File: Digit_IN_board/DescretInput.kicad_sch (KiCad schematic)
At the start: 55 parts, among them J11 DS1013-01-10RSiB-B (1), J12 DS0, J13 DS0

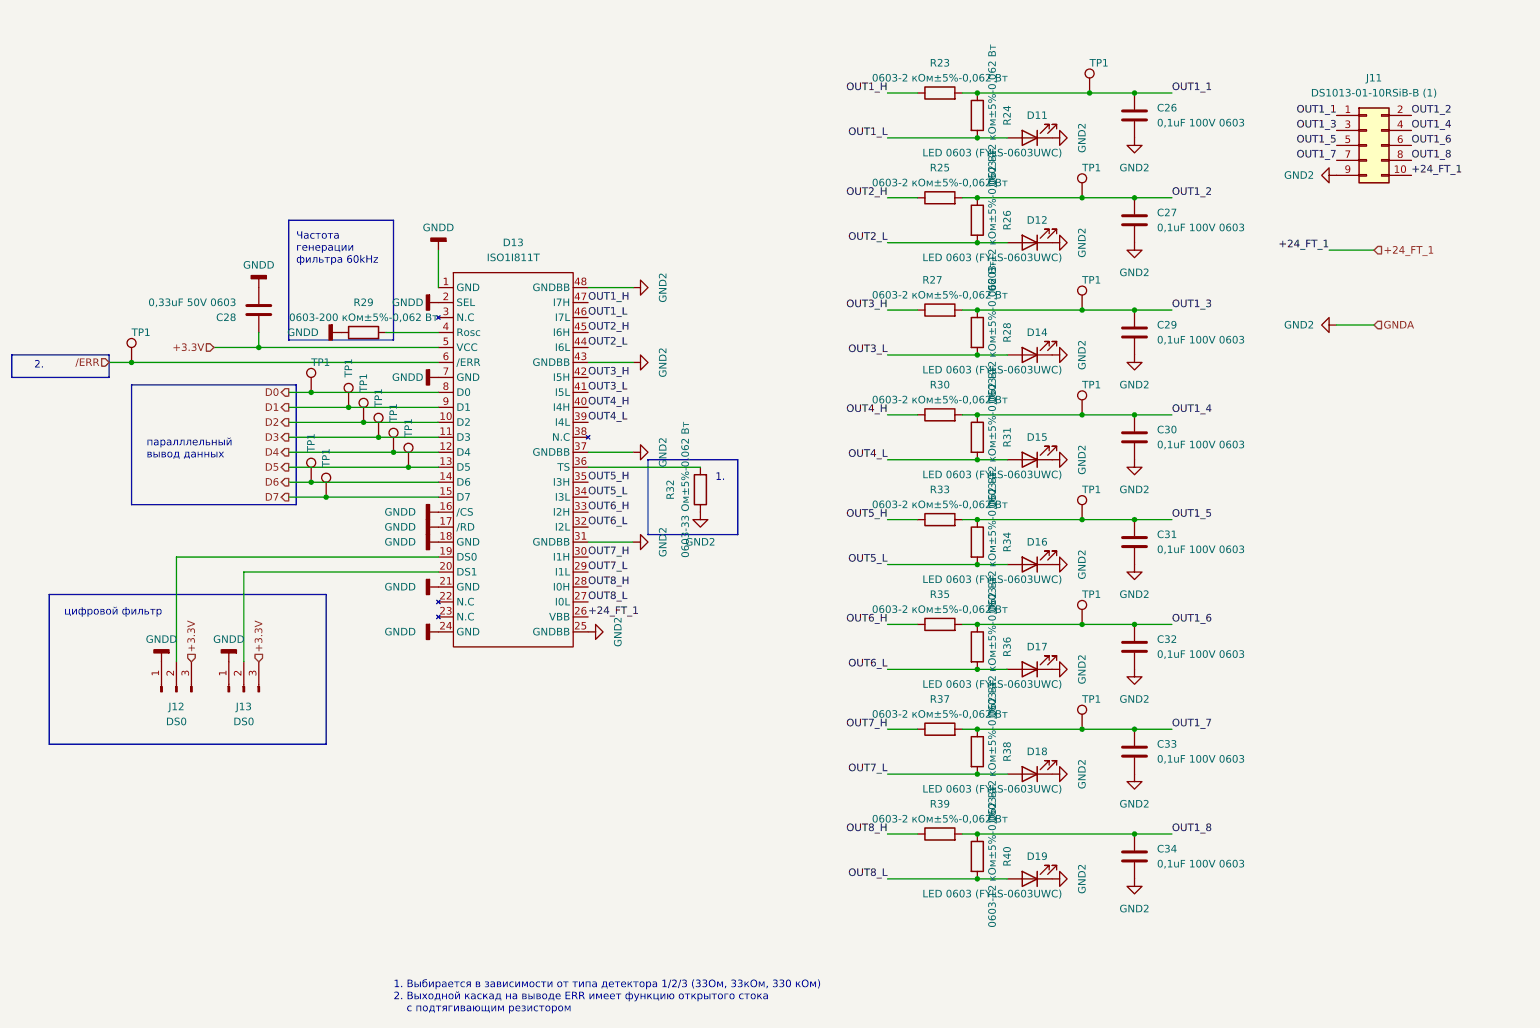
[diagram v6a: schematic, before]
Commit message: fix "pia" typo
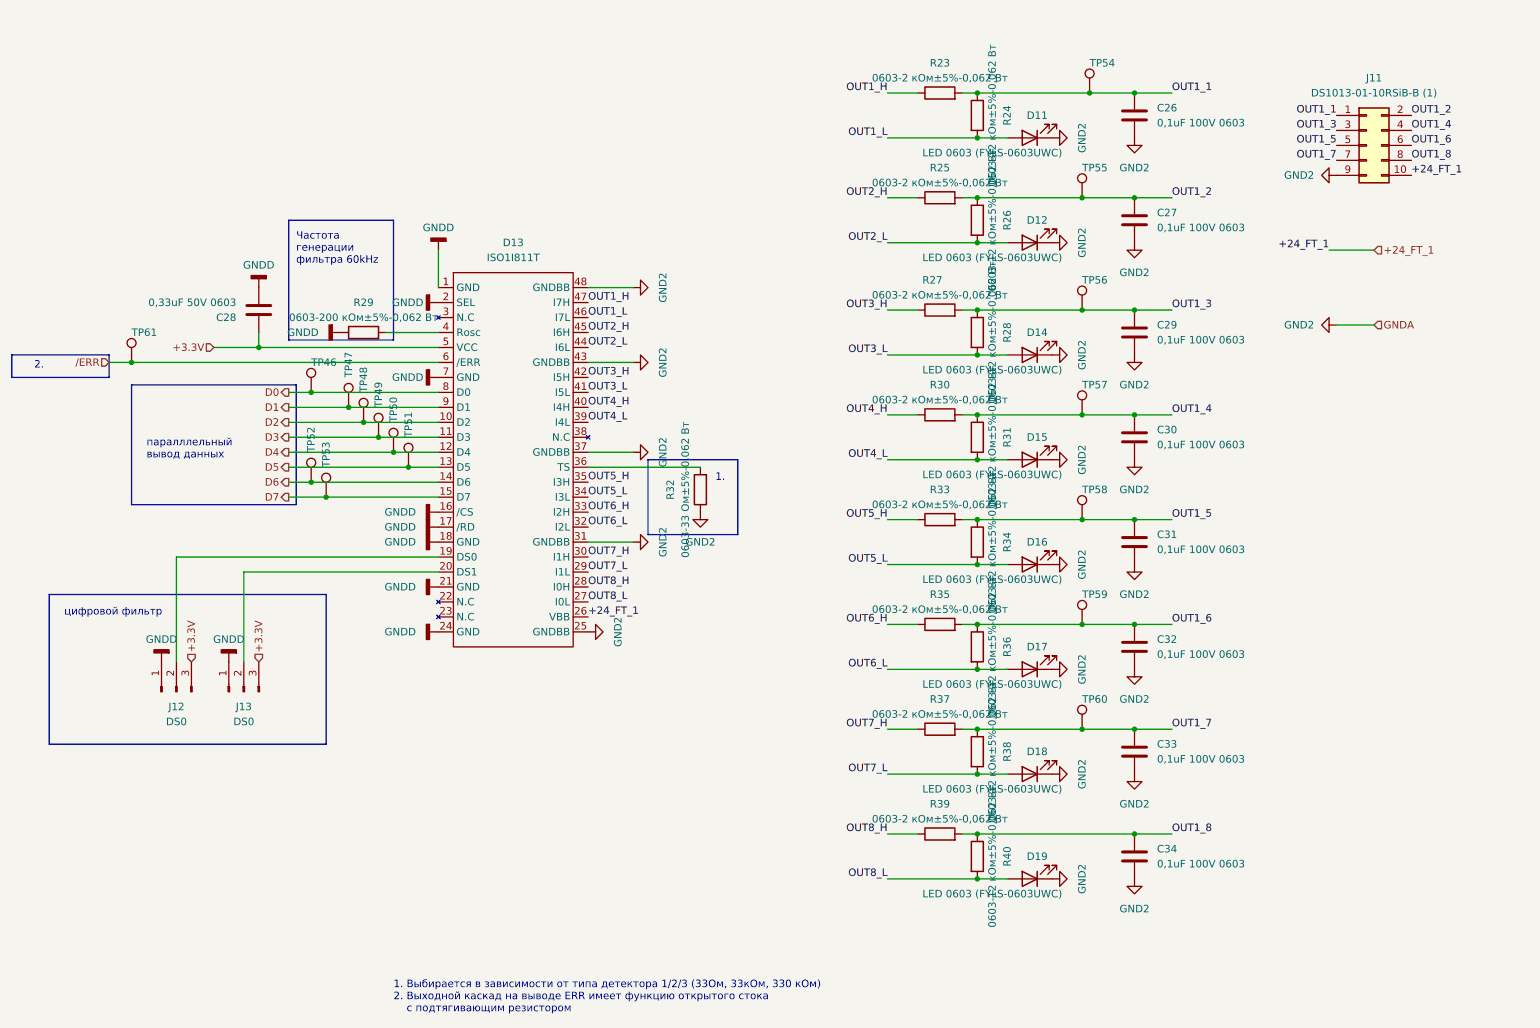
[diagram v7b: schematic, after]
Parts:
- renumbered TP1 to TP46, TP1 to TP47, TP1 to TP48, TP1 to TP49, TP1 to TP50, TP1 to TP51, TP1 to TP52, TP1 to TP53, TP1 to TP54, TP1 to TP55, TP1 to TP56, TP1 to TP57, TP1 to TP58, TP1 to TP59, TP1 to TP60, TP1 to TP61
